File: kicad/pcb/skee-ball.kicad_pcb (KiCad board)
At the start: 2 copper layers, 106 x 106 mm, 62 parts, among them J13 HEADER, J18 DC_DRIVER, J19 JOYSTICK, J2 EXTERNAL_BUTTON, J20 SERVO, J21 US0, J22 US1, J26 US2, J27 US3, J3 Conn_02x06_Counter_Clockwise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

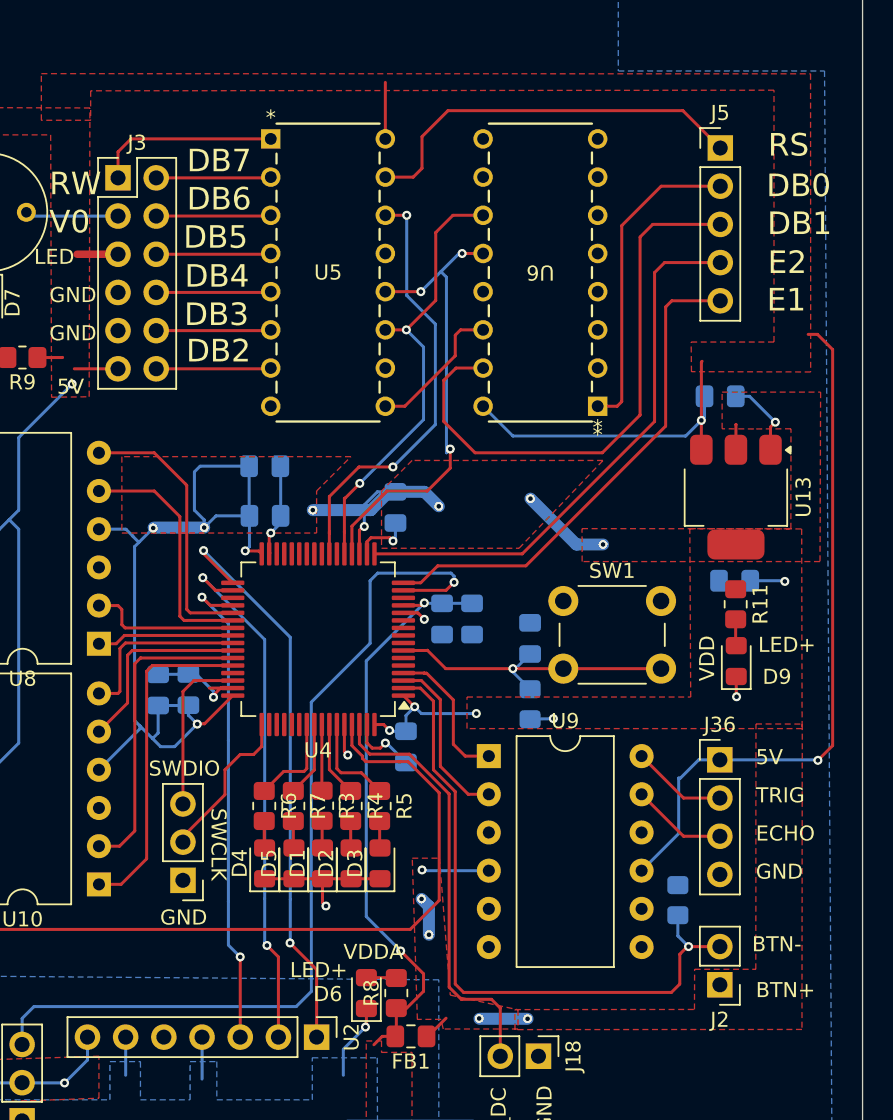
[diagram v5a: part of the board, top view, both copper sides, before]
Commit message: reshape power planes
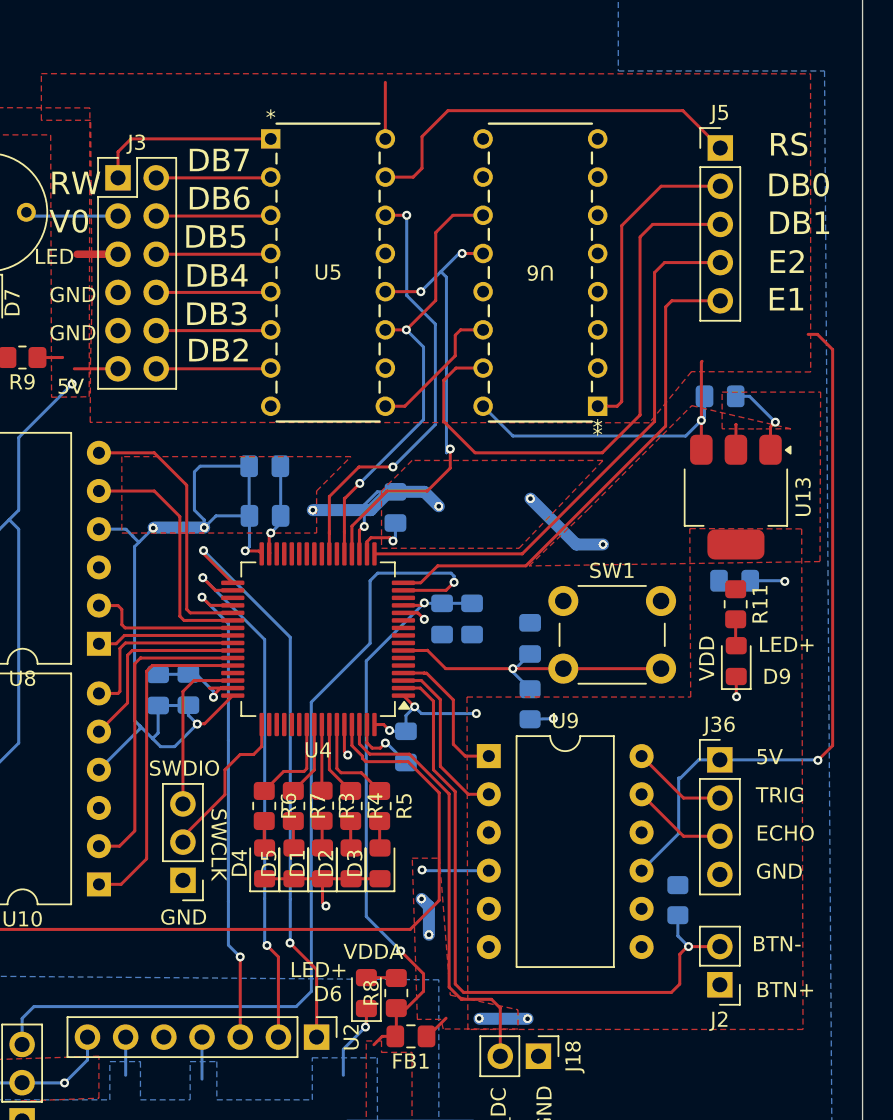
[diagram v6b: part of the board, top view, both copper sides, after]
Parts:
- J3: value Conn_02x06_Counter_Clockwise -> NHD_CONN1
- J5: value Conn_01x05 -> NHD_CONN2
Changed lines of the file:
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@@
 		(rev "2")
 		(company "Purdue University")
-		(comment 1 "Created by Andrew Cali, David Fall, Jennifer Ferguson, and Madeline Flanagan for ECE 47700 Digital Systems Senior Design, Spring 2025.")
+		(comment 1 "Created by Andrew Cali, David Fall, Jennifer Ferguson, and Madeline Flanagan ")
+		(comment 2 "ECE 47700 Digital Systems Senior Design, Spring 2025")
 	)
 	(layers
@@
 			)
 		)
-		(property "Datasheet" ""
+		(property "Datasheet" "~https://engineering.purdue.edu/477grp1/Files/refs/barrel_jack.pdf"
 			(at 0 0 -90)
 			(unlocked yes)
@@
 			)
 		)
-		(property "Datasheet" "http://www.ti.com/lit/ds/symlink/sn74hc595.pdf"
+		(property "Datasheet" "https://engineering.purdue.edu/477grp1/Files/refs/sn74hc595.pdf"
 			(at 0 0 0)
 			(layer "F.Fab")
@@
 			)
 		)
-		(property "Datasheet" ""
+		(property "Datasheet" "https://engineering.purdue.edu/477grp1/Files/refs/bob12009.pdf"
 			(at 0 0 0)
 			(unlocked yes)
@@
 			)
 		)
-		(property "Datasheet" ""
+		(property "Datasheet" "https://engineering.purdue.edu/477grp1/Files/refs/3339P-1-103.pdf"
 			(at 0 0 180)
 			(unlocked yes)
@@
 			)
 		)
-		(property "Datasheet" "https://www.analog.com/media/en/technical-documentation/data-sheets/MAX98357A-MAX98357B.pdf"
+		(property "Datasheet" "https://engineering.purdue.edu/477grp1/Files/refs/max98357.pdf"
 			(at 0 0 -90)
 			(unlocked yes)
@@
 			)
 		)
-		(property "Datasheet" "http://www.st.com/st-web-ui/static/active/en/resource/technical/document/datasheet/CD00000544.pdf"
+		(property "Datasheet" "https://engineering.purdue.edu/477grp1/Files/refs/ld1117.pdf"
 			(at 0 0 -90)
 			(unlocked yes)
@@
 			)
 		)
-		(property "Datasheet" "https://www.st.com/resource/en/datasheet/stm32f091rc.pdf"
+		(property "Datasheet" "https://engineering.purdue.edu/477grp1/Files/refs/stm32f091cc.pdf"
 			(at 0 0 0)
 			(layer "F.Fab")
@@
 			)
 		)
-		(property "Datasheet" "http://www.ti.com/lit/ds/symlink/sn74hc595.pdf"
+		(property "Datasheet" "https://engineering.purdue.edu/477grp1/Files/refs/sn74hc595.pdf"
 			(at 0 0 0)
 			(layer "F.Fab")
@@
 			)
 		)
-		(property "Value" "Conn_01x05"
+		(property "Value" "NHD_CONN2"
 			(at 0 12.49 0)
 			(layer "F.Fab")
@@
 			)
 		)
-		(property "Datasheet" ""
+		(property "Datasheet" "https://engineering.purdue.edu/477grp1/Files/refs/d24v22f6.pdf"
 			(at 0 0 90)
 			(layer "F.Fab")
@@
 			)
 		)
-		(property "Datasheet" ""
+		(property "Datasheet" "https://engineering.purdue.edu/477grp1/Files/refs/bob12009.pdf"
 			(at 0 0 180)
 			(unlocked yes)
@@
 			)
 		)
-		(property "Datasheet" ""
+		(property "Datasheet" "https://engineering.purdue.edu/477grp1/Files/refs/bob12009.pdf"
 			(at 0 0 180)
 			(unlocked yes)
@@
 			)
 		)
-		(property "Datasheet" "http://www.ti.com/lit/gpn/sn74LS08"
+		(property "Datasheet" "https://engineering.purdue.edu/477grp1/Files/refs/sn74hc08.pdf"
 			(at 0 0 90)
 			(layer "F.Fab")
@@
 			)
 		)
-		(property "Value" "Conn_02x06_Counter_Clockwise"
+		(property "Value" "NHD_CONN1"
 			(at 1.27 15.03 0)
 			(layer "F.Fab")
@@
 			)
 		)
-		(property "Datasheet" ""
+		(property "Datasheet" "https://engineering.purdue.edu/477grp1/Files/refs/d24v22f5.pdf"
 			(at 0 0 90)
 			(layer "F.Fab")
@@
 		(polygon
 			(pts
-				(xy 164.21 58.61) (xy 162.1 58.6) (xy 162.1 56.16) (xy 168.65 56.16) (xy 168.61 67.43) (xy 152.79 67.43)
-				(xy 152.78 65.24) (xy 166.67 65.25) (xy 166.68 58.6)
+				(xy 164.21 58.61) (xy 162.1 58.6) (xy 162.1 56.16) (xy 168.65 56.16) (xy 168.61 67.43) (xy 149.26 67.72)
+				(xy 153.18 63.97) (xy 160.08 57.06) (xy 166.68 58.6)
 			)
 		)
@@
 		(polygon
 			(pts
-				(xy 159.95 65.24) (xy 167.39 65.26) (xy 167.42 78.54) (xy 145.13 78.54) (xy 145.13 76.44) (xy 160.01 76.44)
+				(xy 159.95 65.24) (xy 167.39 65.26) (xy 167.48 98.55) (xy 145.19 98.55) (xy 145.13 76.44) (xy 160.01 76.44)
 			)
 		)
@@
 		(polygon
 			(pts
-				(xy 165.55 36.08) (xy 120.1 36.12) (xy 120.1 38.08) (xy 116.82 38.08) (xy 116.82 34.98) (xy 167.98 34.99)
-				(xy 167.99 54.82) (xy 160.06 54.8) (xy 160.04 52.83) (xy 165.55 52.83)
+				(xy 120.09 54.25) (xy 120.19 50.11) (xy 120.1 38.08) (xy 116.82 38.08) (xy 116.82 34.98) (xy 167.98 34.99)
+				(xy 167.99 54.82) (xy 160.06 54.8) (xy 157.27 58.2) (xy 120.07 58.17)
 			)
 		)
@@
 			)
 		)
-	)
-	(zone
-		(net 2)
-		(net_name "VDD")
-		(layer "F.Cu")
-		(hatch edge 0.5)
-		(priority 10)
-		(connect_pads
-			(clearance 0.5)
-		)
-		(min_thickness 0.25)
-		(filled_areas_thickness no)
-		(fill yes
-			(thermal_gap 0.5)
-			(thermal_bridge_width 0.5)
-		)
-		(polygon
-			(pts
-				(xy 167.43 78.24) (xy 167.41 98.55) (xy 148.32 98.56) (xy 148.32 97.23) (xy 160.26 97.22) (xy 160.27 94.55)
-				(xy 164.34 94.55) (xy 164.35 78.23)
-			)
-		)

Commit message: add large vias for debugging
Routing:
- net GND: vias 11 -> 15
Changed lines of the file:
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@@
+		)
+	)
+	(gr_text "GND"
+		(at 160.97 106.1 0)
+		(layer "F.SilkS")
+		(effects
+			(font
+				(size 1.5 1.5)
+				(thickness 0.3)
+				(bold yes)
+			)
+			(justify left bottom)
 		)
 	)
@@
 	)
 	(gr_text "GND"
+		(at 66.95 106 0)
+		(layer "F.SilkS")
+		(effects
+			(font
+				(size 1.5 1.5)
+				(thickness 0.3)
+				(bold yes)
+			)
+			(justify left bottom)
+		)
+	)
+	(gr_text "GND"
 		(at 117.348 50.292 0)
 		(layer "F.SilkS")
@@
 	)
 	(gr_text "GND"
+		(at 145.66 30.72 0)
+		(layer "F.SilkS")
+		(effects
+			(font
+				(size 1.5 1.5)
+				(thickness 0.3)
+				(bold yes)
+			)
+			(justify left bottom)
+		)
+	)
+	(gr_text "GND"
 		(at 83.82 107.188 270)
 		(layer "F.SilkS")
@@
 				(size 1 1)
 				(thickness 0.1875)
+			)
+			(justify left bottom)
+		)
+	)
+	(gr_text "GND"
+		(at 81.58 30.72 0)
+		(layer "F.SilkS")
+		(effects
+			(font
+				(size 1.5 1.5)
+				(thickness 0.3)
+				(bold yes)
 			)
 			(justify left bottom)
@@
 	)
 	(via
+		(at 150.98 28.82)
+		(size 1)
+		(drill 0.7)
+		(layers "F.Cu" "B.Cu")
+		(free yes)
+		(net 3)
+	)
+	(via
+		(at 72.27 105.02)
+		(size 1)
+		(drill 0.7)
+		(layers "F.Cu" "B.Cu")
+		(free yes)
+		(net 3)
+	)
+	(via
 		(at 139.7 79.502)
 		(size 0.6)
@@
 	)
 	(via
+		(at 86.9 28.82)
+		(size 1)
+		(drill 0.7)
+		(layers "F.Cu" "B.Cu")
+		(free yes)
+		(net 3)
+	)
+	(via
 		(at 95.04 79.24)
 		(size 0.6)
@@
 		(net 3)
 	)
+	(via
+		(at 166.29 105.12)
+		(size 1)
+		(drill 0.7)
+		(layers "F.Cu" "B.Cu")
+		(free yes)
+		(net 3)
+	)

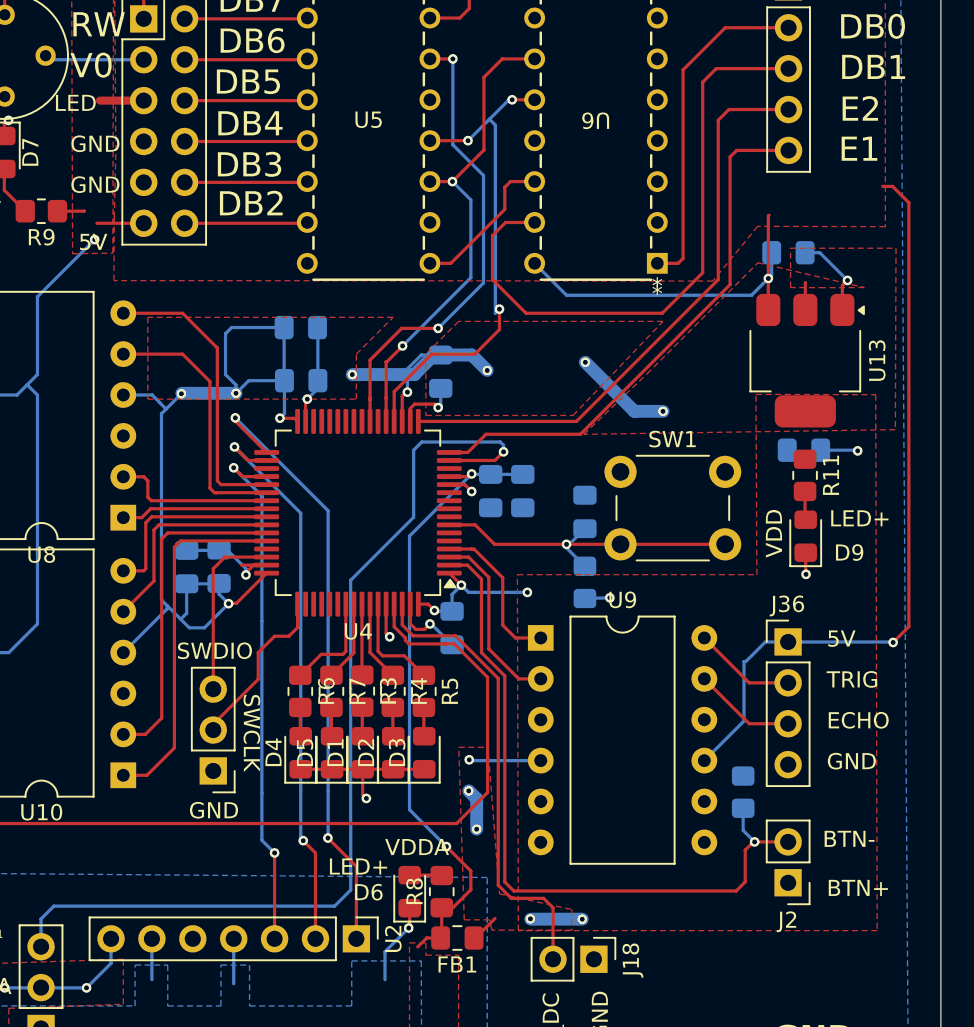
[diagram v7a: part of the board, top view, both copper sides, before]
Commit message: fix analog ground plane connection:
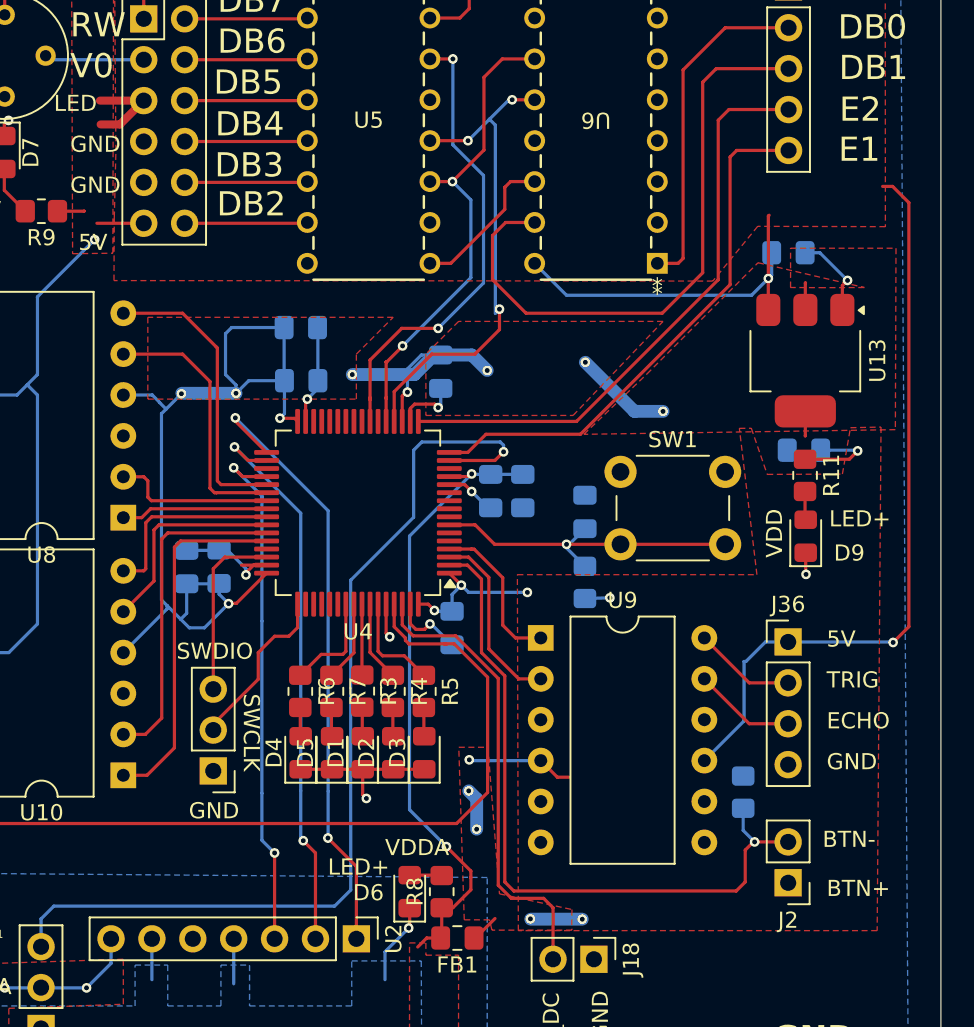
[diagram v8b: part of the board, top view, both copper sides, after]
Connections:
- U4 pad 12: Net-(U4-VSSA) -> GND
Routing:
- net VDD: track 105.3 -> 112.5 mm
- net +5V: track 231.8 -> 235.1 mm
- net GND: track 62.1 -> 65.3 mm, vias 15 -> 16
- net Net-(U4-VSSA): track 1.57 -> 0.00 mm, vias 1 -> 0
